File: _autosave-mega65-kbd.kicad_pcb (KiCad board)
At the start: 2 copper layers, 4 parts, among them U1 PCAL6416AFH, U2 PCAL6416AFH, U3 TCA9555DBR

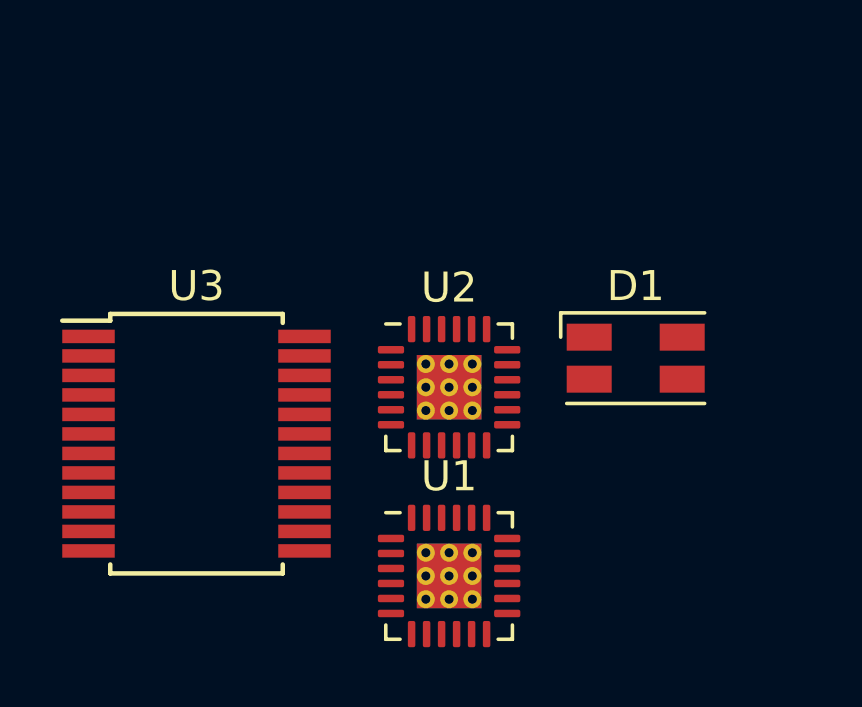
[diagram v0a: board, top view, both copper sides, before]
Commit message: add IO expanders and connect LEDs
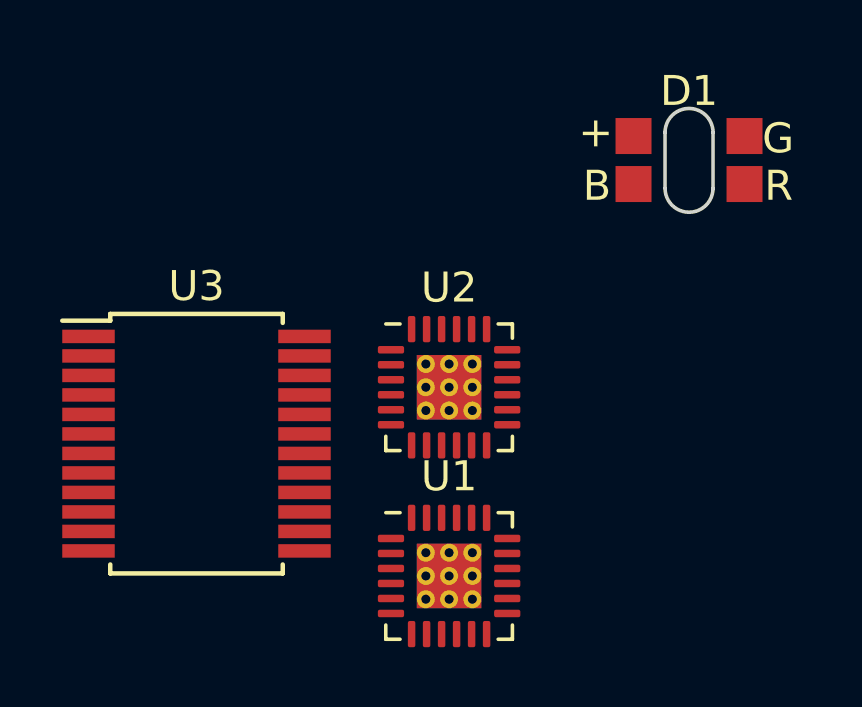
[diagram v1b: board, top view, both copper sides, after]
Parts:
- D1: value LED_RGBK -> LED_RGBK_Wuerth_156120M173000; footprint LED_SMD:LED_RGB_Wuerth-PLCC4_3.2x2.8mm_150141M173100 -> 00Project-LEDs:Wuerth-RGB-LED-156120M173000
- moved D1 6.84 mm to (105.2, 52.8)
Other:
- board outline added: 1.6 x 3.5 mm
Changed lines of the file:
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@@
     )
   )
-  (footprint "LED_SMD:LED_RGB_Wuerth-PLCC4_3.2x2.8mm_150141M173100" (layer "F.Cu")
-    (at 103.378 59.436)
-    (descr "3.2mm x 2.8mm PLCC4 LED, https://www.we-online.de/katalog/datasheet/150141M173100.pdf")
-    (tags "LED RGB Wurth PLCC-4")
+  (footprint "00Project-LEDs:Wuerth-RGB-LED-156120M173000" (layer "F.Cu")
+    (at 105.156 52.832)
+    (descr "RGB LED 3.2x2.7mm http://www.avagotech.com/docs/AV02-0610EN")
+    (tags "LED 3227")
     (property "Sheetfile" "mega65-kbd.kicad_sch")
     (property "Sheetname" "")
     (attr smd)
-    (fp_text reference "D1" (at 0 -2.4) (layer "F.SilkS")
+    (fp_text reference "D1" (at 0 -2.3) (layer "F.SilkS")
       (effects (font (size 1 1) (thickness 0.15)))
     )
-    (fp_text value "LED_RGBK" (at 0 2.5) (layer "F.Fab")
+    (fp_text value "LED_RGBK_Wuerth_156120M173000" (at 0 2.45) (layer "F.Fab")
       (effects (font (size 1 1) (thickness 0.15)))
     )
-    (fp_text user "${REFERENCE}" (at 0 0) (layer "F.Fab")
-      (effects (font (size 0.5 0.5) (thickness 0.075)))
+    (fp_text user "B" (at -3.07 0.86 unlocked) (layer "F.SilkS")
+      (effects (font (size 1 1) (thickness 0.15)))
     )
-    (fp_line (start -2.5 -1.51) (end 2.3 -1.51) (layer "F.SilkS") (width 0.12))
-    (fp_line (start -2.5 -0.7) (end -2.5 -1.51) (layer "F.SilkS") (width 0.12))
-    (fp_line (start -2.3 1.51) (end 2.3 1.51) (layer "F.SilkS") (width 0.12))
-    (fp_line (start -2.55 -1.65) (end -2.55 1.65) (layer "F.CrtYd") (width 0.05))
-    (fp_line (start 2.55 1.65) (end 2.55 -1.65) (layer "F.CrtYd") (width 0.05))
-    (fp_line (start -2.55 1.65) (end 2.55 1.65) (layer "F.CrtYd") (width 0.05))
-    (fp_line (start 2.55 -1.65) (end -2.55 -1.65) (layer "F.CrtYd") (width 0.05))
-    (fp_line (start -0.6 -1.4) (end -1.6 -0.4) (layer "F.Fab") (width 0.1))
-    (fp_line (start -1.6 -1.4) (end -1.6 1.4) (layer "F.Fab") (width 0.1))
-    (fp_line (start 1.6 -1.4) (end -1.6 -1.4) (layer "F.Fab") (width 0.1))
-    (fp_line (start -1.6 1.4) (end 1.6 1.4) (layer "F.Fab") (width 0.1))
-    (fp_line (start 1.6 1.4) (end 1.6 -1.4) (layer "F.Fab") (width 0.1))
-    (fp_circle (center 0 0) (end 1.12 0) (layer "F.Fab") (width 0.1) (fill none))
-    (pad "1" smd rect (at 1.55 -0.7) (size 1.5 0.9) (layers "F.Cu" "F.Paste" "F.Mask")
-      (net 1 "unconnected-(D1-Pad1)") (pinfunction "RA") (pintype "passive"))
-    (pad "2" smd rect (at 1.55 0.7) (size 1.5 0.9) (layers "F.Cu" "F.Paste" "F.Mask")
-      (net 2 "unconnected-(D1-Pad2)") (pinfunction "GA") (pintype "passive"))
-    (pad "3" smd rect (at -1.55 -0.7) (size 1.5 0.9) (layers "F.Cu" "F.Paste" "F.Mask")
-      (net 3 "unconnected-(D1-Pad3)") (pinfunction "BA") (pintype "passive"))
-    (pad "4" smd rect (at -1.55 0.7) (size 1.5 0.9) (layers "F.Cu" "F.Paste" "F.Mask")
-      (net 4 "unconnected-(D1-Pad4)") (pinfunction "K") (pintype "passive"))
-    (model "${KICAD6_3DMODEL_DIR}/LED_SMD.3dshapes/LED_RGB_Wuerth-PLCC4_3.2x2.8mm_150141M173100.wrl"
+    (fp_text user "R" (at 2.99 0.86 unlocked) (layer "F.SilkS")
+      (effects (font (size 1 1) (thickness 0.15)))
+    )
+    (fp_text user "+" (at -3.11 -0.92 unlocked) (layer "F.SilkS")
+      (effects (font (size 1 1) (thickness 0.15)))
+    )
+    (fp_text user "G" (at 2.97 -0.72 unlocked) (layer "F.SilkS")
+      (effects (font (size 1 1) (thickness 0.15)))
+    )
+    (fp_text user "${REFERENCE}" (at 0 -2.3) (layer "F.Fab")
+      (effects (font (size 1 1) (thickness 0.15)))
+    )
+    (fp_line (start 0.8 -0.92) (end 0.8 0.94) (layer "Edge.Cuts") (width 0.12))
+    (fp_line (start -0.8 0.94) (end -0.8 -0.92) (layer "Edge.Cuts") (width 0.12))
+    (fp_arc (start -0.8 -0.92) (mid 0 -1.72) (end 0.8 -0.92) (layer "Edge.Cuts") (width 0.12))
+    (fp_arc (start 0.8 0.94) (mid 0 1.74) (end -0.8 0.94) (layer "Edge.Cuts") (width 0.12))
+    (fp_line (start 2.85 1.65) (end 2.85 -1.65) (layer "F.CrtYd") (width 0.05))
+    (fp_line (start -2.95 -1.65) (end -2.95 1.65) (layer "F.CrtYd") (width 0.05))
+    (fp_line (start 2.85 -1.65) (end -2.95 -1.65) (layer "F.CrtYd") (width 0.05))
+    (fp_line (start -2.95 1.65) (end 2.85 1.65) (layer "F.CrtYd") (width 0.05))
+    (fp_line (start 1.61 0.83) (end -1.59 0.83) (layer "F.Fab") (width 0.1))
+    (fp_line (start -1.6 1.35) (end -1.6 -0.675) (layer "F.Fab") (width 0.1))
+    (fp_line (start -1.2825 -0.74) (end 1.2425 -0.74) (layer "F.Fab") (width 0.1))
+    (fp_line (start 1.6 -1.35) (end 1.6 1.35) (layer "F.Fab") (width 0.1))
+    (pad "1" smd rect (at -1.85 -0.8 180) (size 1.2 1.2) (layers "F.Cu" "F.Paste" "F.Mask")
+      (net 1 "unconnected-(D1-Pad1)") (pinfunction "K") (pintype "passive"))
+    (pad "2" smd rect (at -1.85 0.8 180) (size 1.2 1.2) (layers "F.Cu" "F.Paste" "F.Mask")
+      (net 2 "unconnected-(D1-Pad2)") (pinfunction "BA") (pintype "passive"))
+    (pad "3" smd rect (at 1.85 0.8 180) (size 1.2 1.2) (layers "F.Cu" "F.Paste" "F.Mask")
+      (net 3 "unconnected-(D1-Pad3)") (pinfunction "RA") (pintype "passive"))
+    (pad "4" smd rect (at 1.85 -0.8 180) (size 1.2 1.2) (layers "F.Cu" "F.Paste" "F.Mask")
+      (net 4 "unconnected-(D1-Pad4)") (pinfunction "GA") (pintype "passive"))
+    (model "${KICAD6_3DMODEL_DIR}/LED_SMD.3dshapes/LED_RGB_1210.wrl"
       (offset (xyz 0 0 0))
       (scale (xyz 1 1 1))
